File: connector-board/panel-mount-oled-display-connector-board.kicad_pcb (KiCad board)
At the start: 2 copper layers, 42.9 x 21.1 mm, 3 parts, among them J1 Conn_01x08_Pin, J2 Conn_01x08_Pin, J3 Conn_01x16_Socket

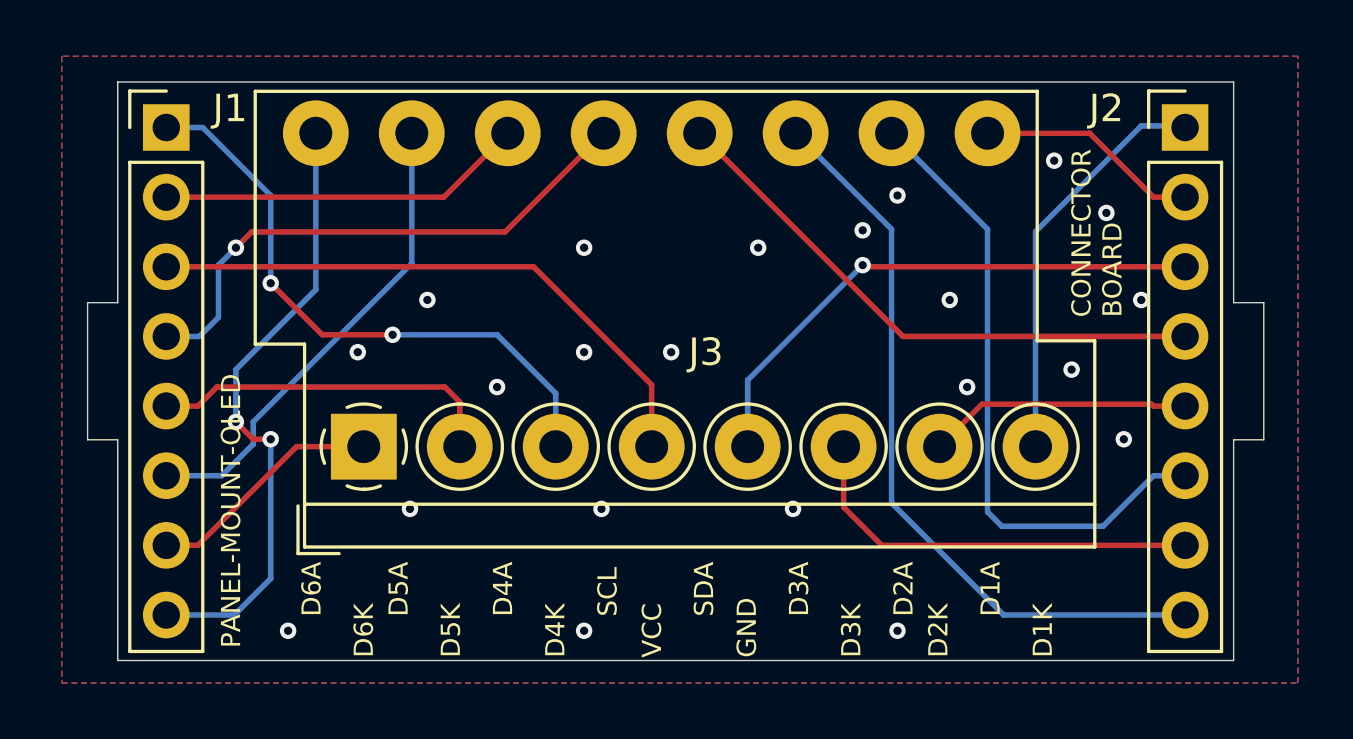
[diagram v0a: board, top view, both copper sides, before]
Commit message: connector: add dual screw-terminal connector options
Add a new connector on the connector board to support either
single-level or two-level screw terminal blocks, providing
flexibility to expose more LEDs when needed.
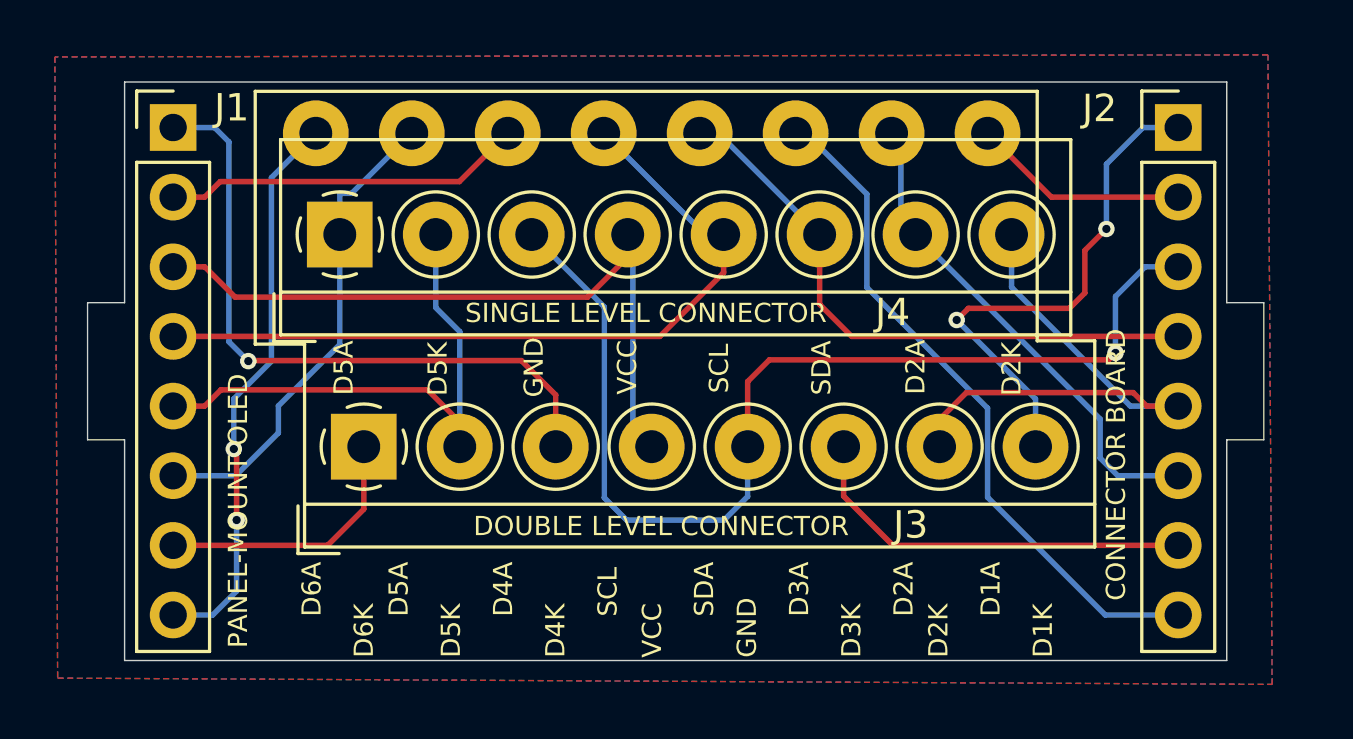
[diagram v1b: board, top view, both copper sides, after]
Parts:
- added J4: Conn_01x08_Socket, TerminalBlock_4Ucon:TerminalBlock_4Ucon_1x08_P3.50mm_Horizontal, F.Cu at (109.2, 105.6)
- moved J1 0.25 mm to (103.1, 101.7)
- moved J2 0.25 mm to (139.8, 101.7)
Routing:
- net GND: track 20.1 -> 40.0 mm, vias 23 -> 1
- net /D2K: track 9.62 -> 20.1 mm
- net /SCL: track 20.1 -> 28.3 mm, vias 1 -> 0
- net /D5K: track 12.8 -> 20.2 mm
- net /D2A: track 23.4 -> 18.1 mm
- net /VCC: track 21.7 -> 26.6 mm
- net /D1K: track 14.9 -> 19.1 mm, vias 0 -> 2
- net /D3A: track 27.3 -> 25.1 mm
- net /D4K: track 22.0 -> 24.2 mm, vias 2 -> 1
- net /D6A: track 22.7 -> 20.7 mm
- net /SDA: track 20.8 -> 22.0 mm
- net /D6K: track 8.70 -> 9.78 mm
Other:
- outline, holes or cut-outs redrawn
- board text added: "DOUBLE LEVEL CONNECTOR"
- board text added: "SINGLE LEVEL CONNECTOR"
